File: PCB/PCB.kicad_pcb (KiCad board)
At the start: 2 copper layers, 11 parts, among them J1 Conn_01x06_Socket, J2 Conn_01x04_Socket, J3 Conn_01x06_Socket, J4 Conn_01x04_Socket, J5 Conn_01x06_Socket, J6 Conn_01x06_Socket, J7 Conn_01x04_Socket, J8 Conn_01x04_Socket, U5 SD1306, U6 SD1309, U8 ESP32-DevKitC

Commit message: Finished layout
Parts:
- removed the J1 at (160.0, 97.3)
- removed the J3 at (166.0, 99.8)
- removed J5, J6: Conn_01x06_Socket, Connector_PinHeader_2.54mm:PinHeader_1x06_P2.54mm_Vertical
- added SW1: SW_Push, Connector_PinHeader_2.54mm:PinHeader_2x01_P2.54mm_Vertical, F.Cu at (135.5, 108.5)
- added SW2: SW_Push, Connector_PinHeader_2.54mm:PinHeader_2x01_P2.54mm_Vertical, F.Cu at (135.5, 101.5)
- added SW3: SW_Push, Connector_PinHeader_2.54mm:PinHeader_2x01_P2.54mm_Vertical, F.Cu at (135.5, 94.5)
- moved J4 94.6 mm to (81.0, 104.5)
- moved J3 86.0 mm to (81.0, 78.0)
- moved U6 85.9 mm to (94.4, 51.0), turned to 90 degrees
- moved J2 84.8 mm to (81.0, 53.4)
- moved U7 72.3 mm to (113.4, 51.0), turned to 90 degrees
- moved U5 35.9 mm to (96.6, 65.4)
- moved J1 22.7 mm to (135.5, 72.9)
- renumbered J2 to J1, J4 to J2, J7 to J3, J8 to J4, U8 to U5, U5 to U6, U6 to U7
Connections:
- J1 pad 2: Net-(J2-Pin_2) -> /CLK1
- J1 pad 3: Net-(J2-Pin_3) -> /DATA1
- J2 pad 2: Net-(J4-Pin_2) -> /CLK2
- J2 pad 3: Net-(J4-Pin_3) -> /DATA2
- J3 pad 2: Net-(J7-Pin_2) -> /CLK3
- J3 pad 3: Net-(J7-Pin_3) -> /DATA3
- J4 pad 2: Net-(J8-Pin_2) -> /CLK4
- J4 pad 3: Net-(J8-Pin_3) -> /DATA4
- U5 pad 10: unconnected-(U8-DAC_2/ADC2_CH9/GPIO26-Pad10) -> /CLK3
- U5 pad 11: unconnected-(U8-ADC2_CH7/GPIO27-Pad11) -> /DATA4
- U5 pad 12: unconnected-(U8-MTMS/GPIO14/ADC2_CH6-Pad12) -> /CLK4
- U5 pad 27: unconnected-(U8-GPIO16-Pad27) -> /BTN1
- U5 pad 28: unconnected-(U8-GPIO17-Pad28) -> /BTN2
- U5 pad 29: unconnected-(U8-GPIO5-Pad29) -> /BTN3
- U5 pad 30: unconnected-(U8-GPIO18-Pad30) -> /DATA1
- U5 pad 31: unconnected-(U8-GPIO19-Pad31) -> /CLK1
- U5 pad 33: unconnected-(U8-GPIO21-Pad33) -> Net-(U5-GPIO21)
- U5 pad 36: unconnected-(U8-GPIO22-Pad36) -> Net-(U5-GPIO22)
- U5 pad 7: unconnected-(U8-32K_XP/GPIO32/ADC1_CH4-Pad7) -> /DATA2
- U5 pad 8: unconnected-(U8-32K_XN/GPIO33/ADC1_CH5-Pad8) -> /CLK2
- U5 pad 9: unconnected-(U8-DAC_1/ADC2_CH8/GPIO25-Pad9) -> /DATA3
- U6 pad 3: unconnected-(U5-SCL-Pad3) -> Net-(U5-GPIO22)
- U6 pad 4: unconnected-(U5-SDA-Pad4) -> Net-(U5-GPIO21)
- U7 pad 3: unconnected-(U6-SCL-Pad3) -> Net-(U5-GPIO22)
- U7 pad 4: unconnected-(U6-SDA-Pad4) -> Net-(U5-GPIO21)
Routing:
- net +3.3V: track 0.00 -> 210.0 mm
- net Net-(U5-GPIO21): track 0.00 -> 60.4 mm
- net Net-(U5-GPIO22): track 0.00 -> 49.6 mm
- net /CLK2: track 0.00 -> 34.8 mm
- net /DATA2: track 0.00 -> 32.1 mm
- net /DATA4: track 0.00 -> 26.1 mm
- net /CLK4: track 0.00 -> 21.3 mm
- net /BTN1: track 0.00 -> 19.7 mm
- net /CLK3: track 0.00 -> 18.8 mm
- net /DATA1: track 0.00 -> 16.7 mm
- net /CLK1: track 0.00 -> 16.7 mm
- net /DATA3: track 0.00 -> 16.7 mm
- net /BTN2: track 0.00 -> 15.4 mm
- net /BTN3: track 0.00 -> 13.6 mm
- added copper zone on F.Cu, net GND
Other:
- board outline added: 67 x 73 mm

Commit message: Put all trace in the front
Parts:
- moved U6 0.19 mm to (94.2, 51.0)
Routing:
- net /CLK4: track 21.3 -> 62.5 mm
- net Net-(U5-GPIO22): track 49.6 -> 59.7 mm
- net +3.3V: track 210.0 -> 219.5 mm
- net /CLK3: track 18.8 -> 27.3 mm
- net Net-(U5-GPIO21): track 60.4 -> 68.2 mm
- net /CLK2: track 34.8 -> 41.7 mm

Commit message: update pcb
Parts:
- U5: footprint PCM_Espressif:ESP32-DevKitC -> _custom-footprint:ESP32-DevKitC
- moved J2 16.6 mm to (90.5, 67.0)
- moved J3 12.4 mm to (90.0, 86.5)
- moved SW1 10.3 mm to (128.5, 101.0)
- moved J1 9.24 mm to (127.5, 77.5)
- moved J4 9.22 mm to (90.0, 102.5)
- moved SW2 9.22 mm to (128.5, 95.5)
- moved SW3 8.32 mm to (128.5, 90.0)
- moved U6 4.19 mm to (96.5, 54.5)
- moved U7 3.50 mm to (113.5, 54.5)
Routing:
- net +3.3V: track 219.5 -> 162.6 mm
- net /CLK2: track 41.7 -> 20.4 mm
- net /DATA2: track 32.1 -> 11.0 mm
- net /CLK4: track 62.5 -> 45.7 mm
- net Net-(U5-GPIO22): track 59.7 -> 48.6 mm
- net Net-(U5-GPIO21): track 68.2 -> 59.5 mm
- net /BTN1: track 19.7 -> 11.7 mm
- net /DATA3: track 16.7 -> 9.04 mm
- net /DATA1: track 16.7 -> 9.32 mm
- net /CLK1: track 16.7 -> 9.32 mm
- net /BTN2: track 15.4 -> 9.07 mm
- net /BTN3: track 13.6 -> 7.24 mm
- net /DATA4: track 26.1 -> 19.8 mm
- net /CLK3: track 27.3 -> 21.8 mm
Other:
- board size 67 x 73 mm -> 46 x 64 mm

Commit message: Fixed spacing and orientation of HX711 pins
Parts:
- moved J1 10.3 mm to (127.5, 67.2)
- moved J4 7.75 mm to (90.0, 110.2), turned to 180 degrees
- moved J3 2.75 mm to (90.0, 89.2), turned to 180 degrees
- moved J2 1.03 mm to (90.2, 68.0), turned to 180 degrees
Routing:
- net +3.3V: track 162.6 -> 243.1 mm
- net /CLK4: track 45.7 -> 19.3 mm
- net /CLK3: track 21.8 -> 7.23 mm
- net /DATA2: track 11.0 -> 21.0 mm
- net /CLK1: track 9.32 -> 19.2 mm
- net /DATA1: track 9.32 -> 18.9 mm
- net /DATA3: track 9.04 -> 7.23 mm
- net /DATA4: track 19.8 -> 18.6 mm
- net Net-(U5-GPIO21): track 59.5 -> 58.8 mm
- net /CLK2: track 20.4 -> 21.0 mm

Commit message: Add capacitor
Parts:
- added C1: 10nf, Capacitor_THT:C_Radial_D5.0mm_H11.0mm_P2.00mm, F.Cu at (125.5, 107.0)
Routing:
- net +3.3V: track 243.1 -> 234.1 mm
- net Net-(U5-GPIO22): track 48.6 -> 47.4 mm
- net /CLK2: track 21.0 -> 22.2 mm
- net /DATA4: track 18.6 -> 19.4 mm
- net /DATA2: track 21.0 -> 21.7 mm
- net Net-(U5-GPIO21): track 58.8 -> 58.2 mm

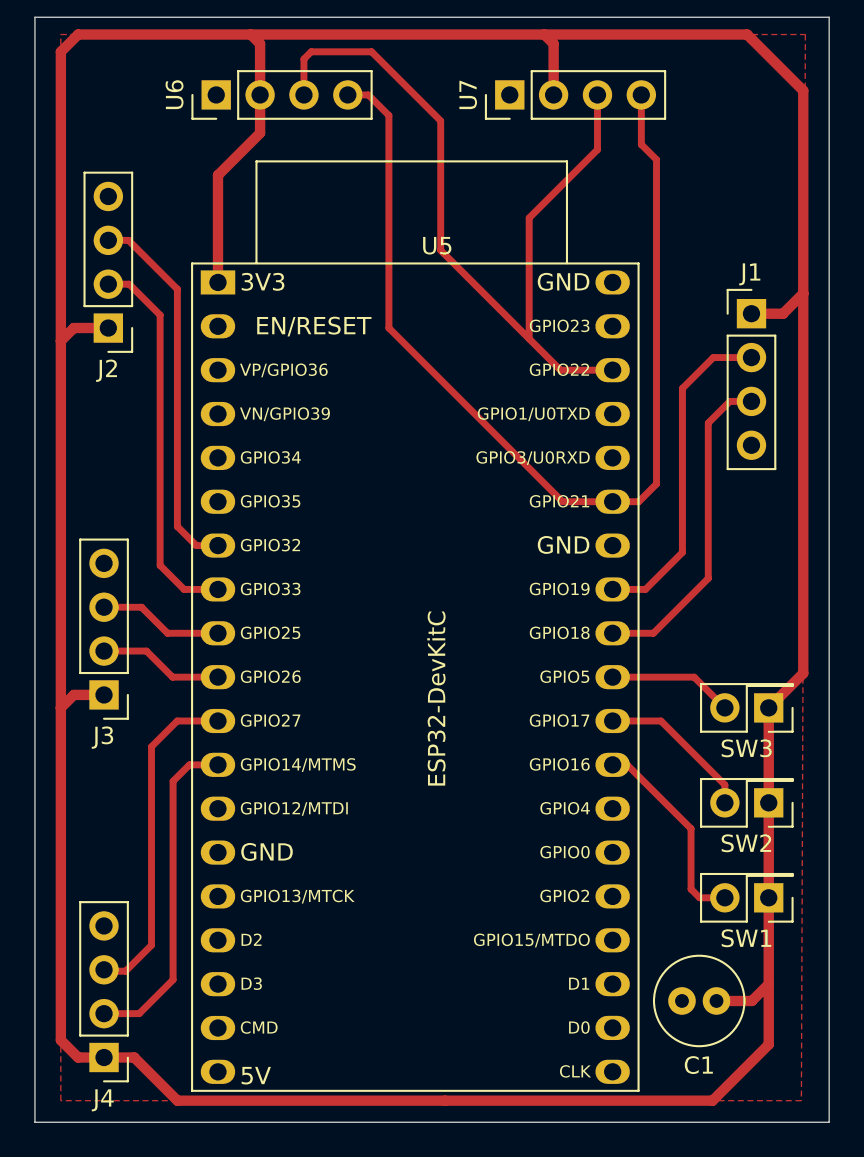
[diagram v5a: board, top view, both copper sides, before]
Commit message: Change push button connection
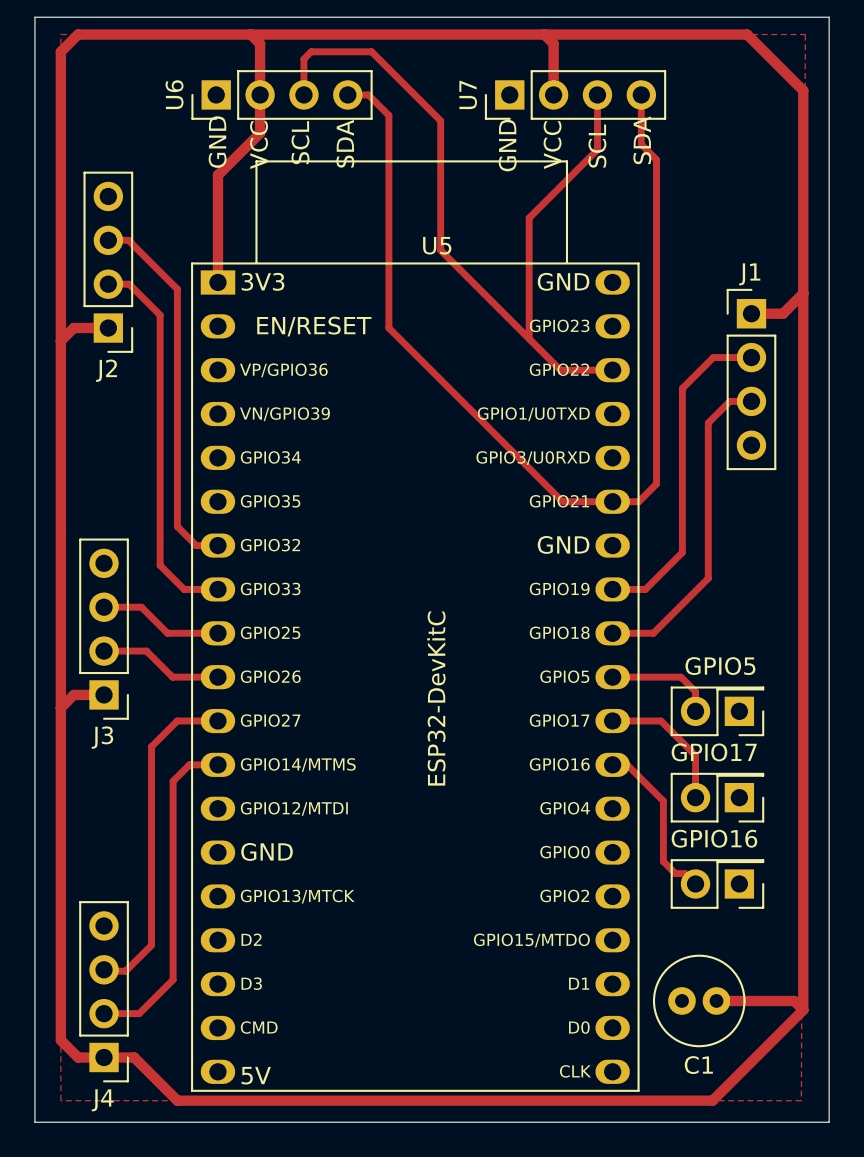
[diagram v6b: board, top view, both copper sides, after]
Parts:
- moved SW1 1.88 mm to (126.8, 100.2)
- moved SW2 1.73 mm to (126.8, 95.2)
- moved SW3 1.71 mm to (126.8, 90.2)
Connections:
- SW1 pad 1: +3.3V -> GND
- SW2 pad 1: +3.3V -> GND
- SW3 pad 1: +3.3V -> GND
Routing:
- net /BTN1: track 11.7 -> 9.71 mm
- net +3.3V: track 234.1 -> 235.9 mm
- net /BTN2: track 9.07 -> 8.07 mm
- net /BTN3: track 7.24 -> 6.29 mm
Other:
- board text added: "GND"
- board text added: "GPIO16"
- board text added: "GPIO17"
- board text added: "GPIO5"
- board text added: "SCL"
- board text added: "SDA"
- board text added: "VCC"
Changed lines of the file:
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@@
 	(footprint "Connector_PinHeader_2.54mm:PinHeader_2x01_P2.54mm_Vertical"
 		(layer "F.Cu")
-		(at 128.5 101 180)
+		(at 126.8 100.2 180)
 		(descr "Through hole straight pin header, 2x01, 2.54mm pitch, double rows")
 		(tags "Through hole pin header THT 2x01 2.54mm double row")
@@
 			(at 1.27 -2.38 0)
 			(layer "F.SilkS")
+			(hide yes)
 			(effects
 				(font
@@
 			(layers "*.Cu" "*.Mask")
 			(remove_unused_layers no)
-			(net "+3.3V")
+			(net "GND")
 			(pinfunction "1_1")
 			(pintype "passive")
@@
 	(footprint "Connector_PinHeader_2.54mm:PinHeader_2x01_P2.54mm_Vertical"
 		(layer "F.Cu")
-		(at 128.5 95.5 180)
+		(at 126.8 95.2 180)
 		(descr "Through hole straight pin header, 2x01, 2.54mm pitch, double rows")
 		(tags "Through hole pin header THT 2x01 2.54mm double row")
@@
 			(at 1.27 -2.38 0)
 			(layer "F.SilkS")
+			(hide yes)
 			(effects
 				(font
@@
 			(layers "*.Cu" "*.Mask")
 			(remove_unused_layers no)
-			(net "+3.3V")
+			(net "GND")
 			(pinfunction "1_1")
 			(pintype "passive")
@@
 	(footprint "Connector_PinHeader_2.54mm:PinHeader_2x01_P2.54mm_Vertical"
 		(layer "F.Cu")
-		(at 128.5 90 180)
+		(at 126.8 90.2 180)
 		(descr "Through hole straight pin header, 2x01, 2.54mm pitch, double rows")
 		(tags "Through hole pin header THT 2x01 2.54mm double row")
@@
 			(at 1.27 -2.38 0)
 			(layer "F.SilkS")
+			(hide yes)
 			(effects
 				(font
@@
 			(layers "*.Cu" "*.Mask")
 			(remove_unused_layers no)
-			(net "+3.3V")
+			(net "GND")
 			(pinfunction "1_1")
 			(pintype "passive")
@@
 		(layer "Edge.Cuts")
 	)
+	(gr_text "GPIO17"
+		(at 122.8 93.2 0)
+		(layer "F.SilkS")
+		(effects
+			(font
+				(size 1 1)
+				(thickness 0.1)
+			)
+			(justify left bottom)
+		)
+	)
+	(gr_text "GPIO16"
+		(at 122.8 98.2 0)
+		(layer "F.SilkS")
+		(effects
+			(font
+				(size 1 1)
+				(thickness 0.1)
+			)
+			(justify left bottom)
+		)
+	)
+	(gr_text "GPIO5"
+		(at 123.6 88.2 0)
+		(layer "F.SilkS")
+		(effects
+			(font
+				(size 1 1)
+				(thickness 0.1)
+			)
+			(justify left bottom)
+		)
+	)
+	(gr_text "GND"
+		(at 97.2 58.8 90)
+		(layer "F.SilkS")
+		(effects
+			(font
+				(size 1 1)
+				(thickness 0.1)
+			)
+			(justify left bottom)
+		)
+	)
+	(gr_text "VCC"
+		(at 99.6 58.8 90)
+		(layer "F.SilkS")
+		(effects
+			(font
+				(size 1 1)
+				(thickness 0.1)
+			)
+			(justify left bottom)
+		)
+	)
+	(gr_text "SCL"
+		(at 102 58.6 90)
+		(layer "F.SilkS")
+		(effects
+			(font
+				(size 1 1)
+				(thickness 0.1)
+			)
+			(justify left bottom)
+		)
+	)
+	(gr_text "SDA"
+		(at 104.6 58.8 90)
+		(layer "F.SilkS")
+		(effects
+			(font
+				(size 1 1)
+				(thickness 0.1)
+			)
+			(justify left bottom)
+		)
+	)
+	(gr_text "GND"
+		(at 114 59 90)
+		(layer "F.SilkS")
+		(effects
+			(font
+				(size 1 1)
+				(thickness 0.1)
+			)
+			(justify left bottom)
+		)
+	)
+	(gr_text "VCC"
+		(at 116.6 58.8 90)
+		(layer "F.SilkS")
+		(effects
+			(font
+				(size 1 1)
+				(thickness 0.1)
+			)
+			(justify left bottom)
+		)
+	)
+	(gr_text "SCL"
+		(at 119.2 58.8 90)
+		(layer "F.SilkS")
+		(effects
+			(font
+				(size 1 1)
+				(thickness 0.1)
+			)
+			(justify left bottom)
+		)
+	)
+	(gr_text "SDA"
+		(at 121.8 58.6 90)
+		(layer "F.SilkS")
+		(effects
+			(font
+				(size 1 1)
+				(thickness 0.1)
+			)
+			(justify left bottom)
+		)
+	)
 	(segment
 		(start 115.5 51)
@@
 	)
 	(segment
-		(start 128.5 101)
-		(end 128.5 95.5)
+		(start 91.75 110.25)
+		(end 90 110.25)
 		(width 0.6)
 		(layer "F.Cu")
@@
 	)
 	(segment
+		(start 130.5 66)
+		(end 130.5 107.5)
+		(width 0.6)
+		(layer "F.Cu")
+		(net "+3.3V")
+	)
+	(segment
 		(start 99.04 54.5)
 		(end 99.04 51.54)
@@
 	)
 	(segment
-		(start 90 110.25)
+		(start 94.25 112.75)
 		(end 91.75 110.25)
-		(width 0.6)
-		(layer "F.Cu")
-		(net "+3.3V")
-	)
-	(segment
-		(start 128.5 106)
-		(end 128.5 101)
-		(width 0.6)
-		(layer "F.Cu")
-		(net "+3.3V")
-	)
-	(segment
-		(start 128.5 95.5)
-		(end 128.5 90)
 		(width 0.6)
 		(layer "F.Cu")
@@
 	)
 	(segment
-		(start 125.25 112.75)
-		(end 128.5 109.5)
-		(width 0.6)
-		(layer "F.Cu")
-		(net "+3.3V")
-	)
-	(segment
 		(start 96.6 65.36)
 		(end 96.6 59.15)
@@
 	)
 	(segment
-		(start 128.5 109.5)
-		(end 128.5 106)
-		(width 0.6)
-		(layer "F.Cu")
-		(net "+3.3V")
-	)
-	(segment
 		(start 130.5 66)
 		(end 130.5 54.25)
@@
 	)
 	(segment
+		(start 125.475 106.975)
+		(end 129.975 106.975)
+		(width 0.6)
+		(layer "F.Cu")
+		(net "+3.3V")
+	)
+	(segment
 		(start 88.5 51)
 		(end 87.5 52)
@@
 	)
 	(segment
-		(start 130.5 88)
-		(end 130.5 66)
-		(width 0.6)
-		(layer "F.Cu")
-		(net "+3.3V")
-	)
-	(segment
 		(start 99.04 51.54)
 		(end 98.5 51)
@@
 	)
 	(segment
-		(start 127.525 106.975)
-		(end 128.5 106)
-		(width 0.6)
-		(layer "F.Cu")
-		(net "+3.3V")
-	)
-	(segment
 		(start 87.5 90)
 		(end 87.5 109.25)
@@
 	)
 	(segment
-		(start 128.5 90)
-		(end 130.5 88)
-		(width 0.6)
-		(layer "F.Cu")
-		(net "+3.3V")
-	)
-	(segment
 		(start 87.5 52)
 		(end 87.5 68.75)
@@
 	)
 	(segment
+		(start 129.975 106.975)
+		(end 130.5 107.5)
+		(width 0.6)
+		(layer "F.Cu")
+		(net "+3.3V")
+	)
+	(segment
 		(start 116.04 54.5)
 		(end 116.04 51.54)
@@
 	)
 	(segment
-		(start 125.475 106.975)
-		(end 127.525 106.975)
-		(width 0.6)
-		(layer "F.Cu")
-		(net "+3.3V")
-	)
-	(segment
-		(start 109.75 112.75)
-		(end 125.25 112.75)
-		(width 0.6)
-		(layer "F.Cu")
-		(net "+3.3V")
-	)
-	(segment
 		(start 115.96 54.42)
 		(end 116.04 54.5)
@@
 	)
 	(segment
-		(start 91.75 110.25)
-		(end 94.25 112.75)
-		(width 0.6)
-		(layer "F.Cu")
-		(net "+3.3V")
-	)
-	(segment
-		(start 94.25 112.75)
-		(end 109.75 112.75)
+		(start 130.5 107.5)
+		(end 125.25 112.75)
 		(width 0.6)
 		(layer "F.Cu")
@@
 	)
 	(segment
+		(start 125.25 112.75)
+		(end 94.25 112.75)
+		(width 0.6)
+		(layer "F.Cu")
+		(net "+3.3V")
+	)
+	(segment
 		(start 98.5 51)
 		(end 88.5 51)
@@
 	)
 	(segment
-		(start 120.3 93.3)
-		(end 124 97)
-		(width 0.4)
-		(layer "F.Cu")
-		(net "/BTN1")
-	)
-	(segment
 		(start 119.46 93.3)
 		(end 120.3 93.3)
@@
 	)
 	(segment
-		(start 124 97)
-		(end 124 100.5)
+		(start 120.3 93.3)
+		(end 122.4 95.4)
 		(width 0.4)
 		(layer "F.Cu")
@@
 	)
 	(segment
-		(start 124 100.5)
-		(end 124.5 101)
+		(start 122.4 95.4)
+		(end 122.4 98.9)
 		(width 0.4)
 		(layer "F.Cu")
@@
 	)
 	(segment
-		(start 124.5 101)
-		(end 125.96 101)
+		(start 123.1 99.6)
+		(end 123.66 99.6)
 		(width 0.4)
 		(layer "F.Cu")
 		(net "/BTN1")
+	)
+	(segment
+		(start 123.66 99.6)
+		(end 124.26 100.2)
+		(width 0.4)
+		(layer "F.Cu")
+		(net "/BTN1")
+	)
+	(segment
+		(start 122.4 98.9)
+		(end 123.1 99.6)
+		(width 0.4)
+		(layer "F.Cu")
+		(net "/BTN1")
+	)
+	(segment
+		(start 124.26 92.76)
+		(end 122.26 90.76)
+		(width 0.4)
+		(layer "F.Cu")
+		(net "/BTN2")
+	)
+	(segment
+		(start 124.26 95.2)
+		(end 124.26 92.76)
+		(width 0.4)
+		(layer "F.Cu")
+		(net "/BTN2")
 	)
 	(segment
@@
 	)
 	(segment
-		(start 125.96 95.5)
-		(end 125.96 94.46)
-		(width 0.4)
-		(layer "F.Cu")
-		(net "/BTN2")
-	)
-	(segment
-		(start 125.96 94.46)
-		(end 122.26 90.76)
-		(width 0.4)
-		(layer "F.Cu")
-		(net "/BTN2")
-	)
-	(segment
-		(start 124.18 88.22)
+		(start 124.26 90.2)
+		(end 124.26 89.06)
+		(width 0.4)
+		(layer "F.Cu")
+		(net "/BTN3")
+	)
+	(segment
+		(start 123.42 88.22)
 		(end 119.46 88.22)
 		(width 0.4)
@@
 	)
 	(segment
-		(start 125.96 90)
-		(end 124.18 88.22)
-		(width 0.4)
-		(layer "F.Cu")
+		(start 124.26 89.06)
+		(end 123.42 88.22)
+		(width 0.4)
+		(layer "F.Cu")

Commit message: backup before routing hw debouncer
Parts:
- added C2: 0.1uf, Capacitor_THT:C_Radial_D5.0mm_H11.0mm_P2.00mm, F.Cu at (148.5, 67.2)
- added C3: 0.1uf, Capacitor_THT:C_Radial_D5.0mm_H11.0mm_P2.00mm, F.Cu at (148.5, 73.8)
- added JP1: Short this route to use software deboucer, Jumper:SolderJumper-2_P1.3mm_Open_Pad1.0x1.5mm, F.Cu at (123.5, 103.0)
- added JP2: Short this route to use software deboucer, Jumper:SolderJumper-2_P1.3mm_Open_Pad1.0x1.5mm, F.Cu at (144.0, 96.0)
- added JP3: Short this route to use software deboucer, Jumper:SolderJumper-2_P1.3mm_Open_Pad1.0x1.5mm, F.Cu at (144.0, 99.5)
- added R1: 1kΩ, Resistor_THT:R_Axial_DIN0207_L6.3mm_D2.5mm_P10.16mm_Horizontal, F.Cu at (134.5, 66.0)
- added R2: 10kΩ, Resistor_THT:R_Axial_DIN0207_L6.3mm_D2.5mm_P10.16mm_Horizontal, F.Cu at (134.5, 70.0)
- added R3: 1kΩ, Resistor_THT:R_Axial_DIN0207_L6.3mm_D2.5mm_P10.16mm_Horizontal, F.Cu at (134.5, 74.1)
- added R4: 10kΩ, Resistor_THT:R_Axial_DIN0207_L6.3mm_D2.5mm_P10.16mm_Horizontal, F.Cu at (134.5, 78.1)
- added R5: 1kΩ, Resistor_THT:R_Axial_DIN0207_L6.3mm_D2.5mm_P10.16mm_Horizontal, F.Cu at (134.5, 82.2)
- added R6: 10kΩ, Resistor_THT:R_Axial_DIN0207_L6.3mm_D2.5mm_P10.16mm_Horizontal, F.Cu at (134.5, 86.2)
- C1: value 10nf -> 0.1uf
- moved SW2 26.9 mm to (148.5, 79.3), turned to 0 degrees
- moved SW3 22.6 mm to (148.5, 83.9), turned to 0 degrees
- moved C1 14.3 mm to (139.4, 103.8)
- moved SW1 5.38 mm to (127.4, 105.5), turned to 90 degrees
- moved J2 4.05 mm to (90.2, 64.0)
- moved J3 2.15 mm to (90.0, 87.1)
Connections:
- C1 pad 1: +3.3V -> /BTN1
- SW1 pad 2: /BTN1 -> Net-(JP1-A)
- SW2 pad 2: /BTN2 -> Net-(JP2-A)
- SW3 pad 2: /BTN3 -> Net-(JP3-A)
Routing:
- net /BTN2: track 8.07 -> 0.00 mm
- net /BTN3: track 6.29 -> 0.00 mm
- net +3.3V: track 235.9 -> 231.1 mm
- net /DATA2: track 21.7 -> 26.1 mm
- net /CLK2: track 22.2 -> 26.3 mm
- net Net-(JP1-A): track 0.00 -> 3.22 mm
- net /BTN1: track 9.71 -> 12.5 mm
- net /DATA3: track 7.23 -> 8.12 mm
- net /CLK3: track 7.23 -> 8.12 mm

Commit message: pcb edits
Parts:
- C1, C2, C3, R1, R2, R3, R4, R5, R6: moved to B.Cu
- moved C2 54.0 mm to (102.5, 95.5), turned to 180 degrees
- moved R1 47.3 mm to (116.0, 109.5), turned to 180 degrees
- moved C3 46.3 mm to (103.0, 82.5), turned to 180 degrees
- moved R2 39.5 mm to (116.1, 105.0), turned to 180 degrees
- moved C1 37.3 mm to (102.5, 109.0)
- moved R3 29.8 mm to (116.1, 97.5), turned to 180 degrees
- moved SW2 28.4 mm to (128.0, 99.0), turned to 90 degrees
- moved JP3 24.8 mm to (128.0, 80.5)
- moved R4 23.3 mm to (116.1, 92.5), turned to 180 degrees
- moved SW3 20.7 mm to (128.0, 86.5), turned to 90 degrees
- moved R6 19.6 mm to (116.1, 79.5), turned to 180 degrees
- moved R5 18.6 mm to (116.1, 85.0), turned to 180 degrees
- moved JP2 16.2 mm to (128.0, 93.5)
- moved SW1 5.24 mm to (124.0, 109.5)
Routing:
- net +3.3V: track 231.1 -> 286.6 mm
- net /BTN3: track 0.00 -> 43.9 mm
- net /BTN2: track 0.00 -> 31.6 mm
- net /BTN1: track 12.5 -> 41.3 mm
- net Net-(JP2-A): track 0.00 -> 20.7 mm
- net Net-(JP3-A): track 0.00 -> 16.1 mm
- net Net-(JP1-A): track 3.22 -> 13.6 mm
